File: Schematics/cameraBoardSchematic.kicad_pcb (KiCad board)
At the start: 2 copper layers, 53 parts, among them IC1 LM3940IS-3.3_NOPB, J1 Runcam Split 4 v2, J2 USB_C_Receptacle, J4 Runcam Split 4 v2, J5 Runcam Split 4 v2, SW1 SW_Push, SW2 SW_Push, U1 STM32F405RGTx, U2 TPS22917DBVR, U3 TPS22917DBVR, U4 SN65HVD230DR, U6 TPS22917DBVR

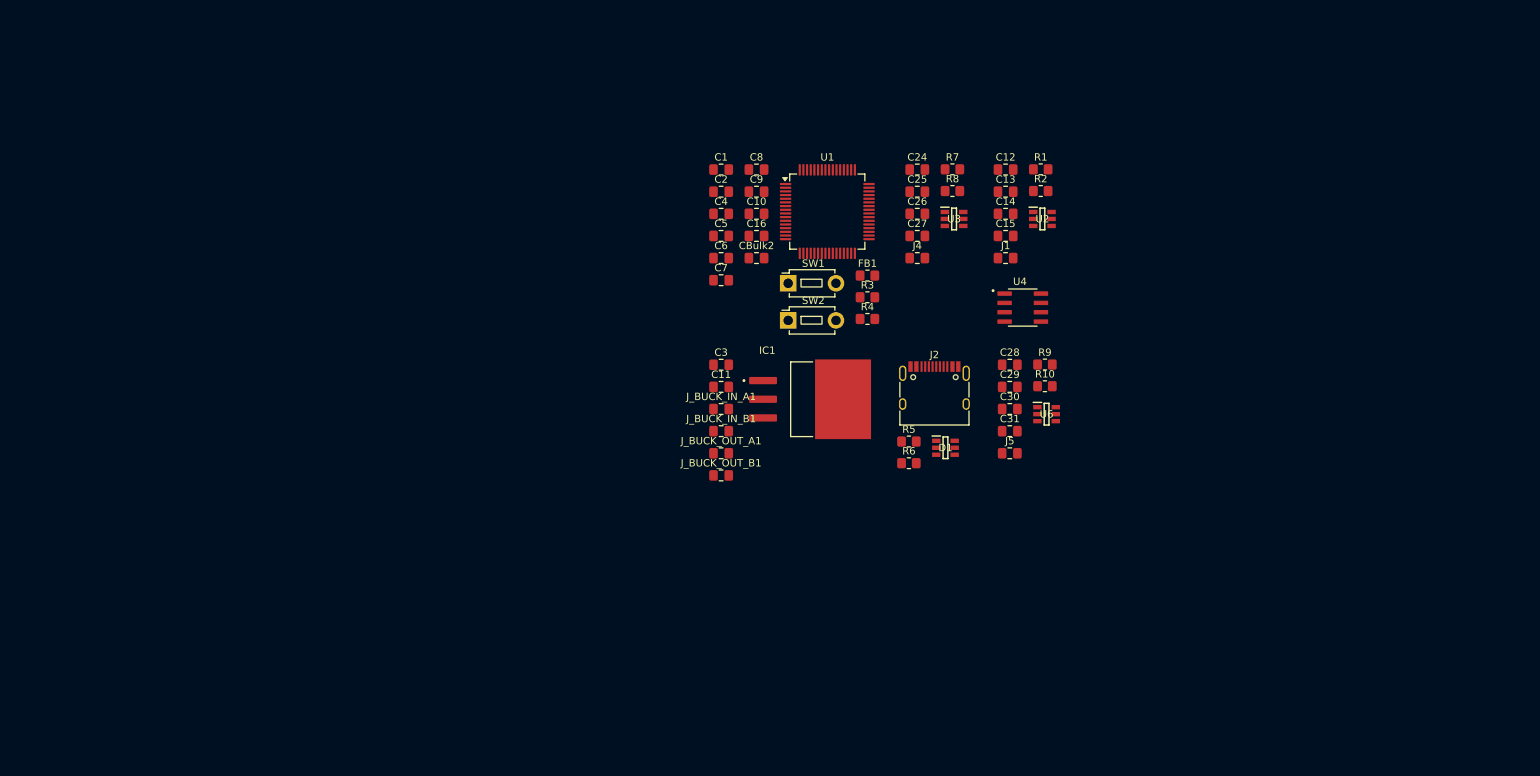
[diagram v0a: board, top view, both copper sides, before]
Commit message: Fixed footprint assignments pcb dev begining
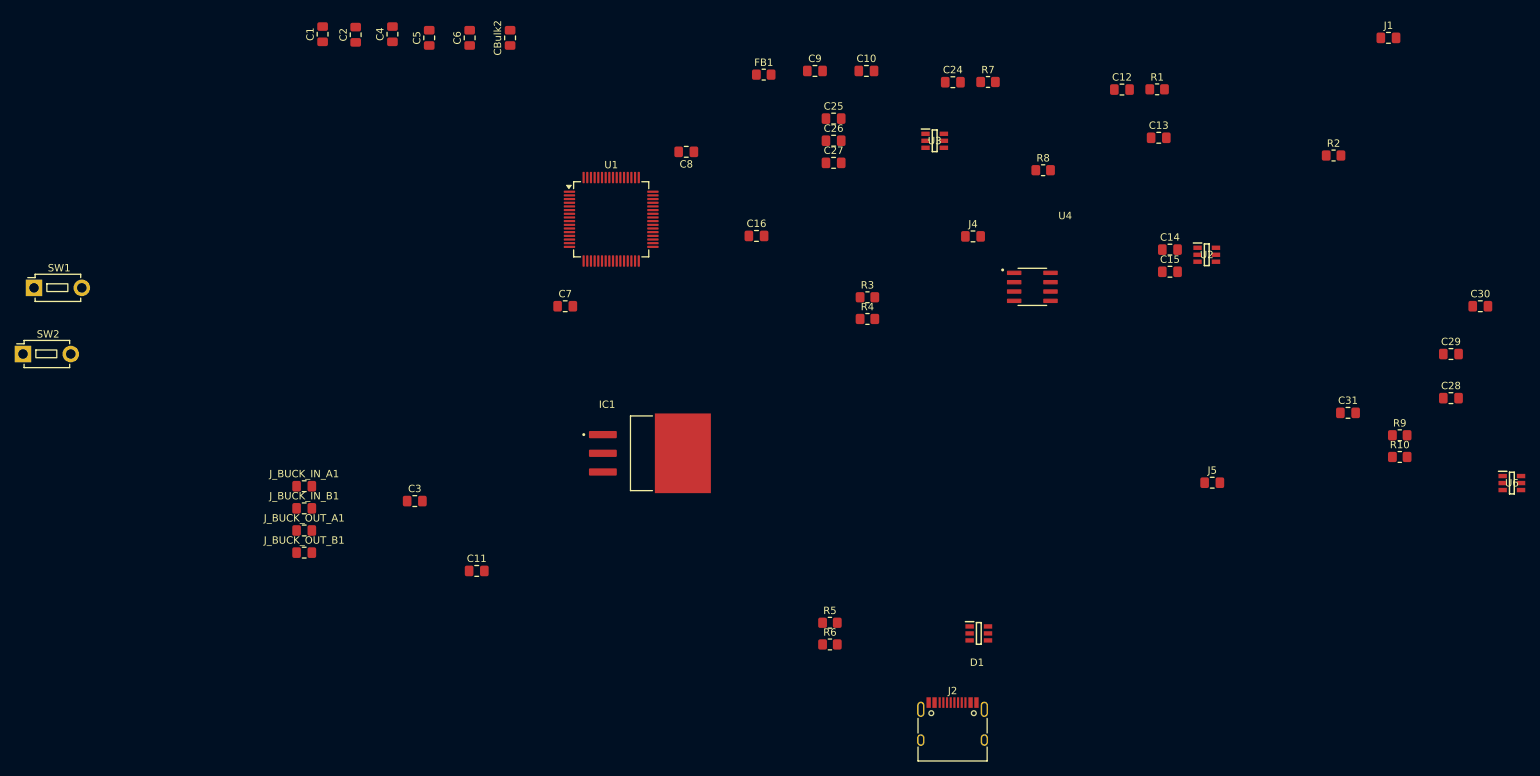
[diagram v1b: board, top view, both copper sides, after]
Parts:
- moved SW2 104.2 mm to (27.8, 95.5)
- moved SW1 102.6 mm to (29.2, 86.5)
- moved C30 65.5 mm to (226.0, 89.0)
- moved U6 64.0 mm to (230.2, 113.0)
- moved C28 60.2 mm to (222.0, 101.5)
- moved C29 60.2 mm to (222.0, 95.5)
- moved J1 60.1 mm to (213.5, 52.5)
- moved J_BUCK_IN_A1 57.7 mm to (66.0, 113.5)
- moved J_BUCK_IN_B1 57.7 mm to (66.0, 116.5)
- moved J_BUCK_OUT_A1 57.7 mm to (66.0, 119.5)
- moved J_BUCK_OUT_B1 57.7 mm to (66.0, 122.5)
- moved C1 57.2 mm to (68.5, 52.0), turned to 90 degrees
- moved C2 54.1 mm to (73.0, 52.1), turned to 90 degrees
- moved C4 50.9 mm to (78.0, 52.0), turned to 90 degrees
- moved R10 49.2 mm to (215.0, 109.5)
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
